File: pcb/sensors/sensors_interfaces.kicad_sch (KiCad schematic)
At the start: 26 parts, among them J3 CAN BUS, J4 DIMMER / GROVE, J5 XDB401 / GROVE, J6 DIGMESA / FLOW, J7 M5STACK VALVE SSR, J8 BOILER SSR / 5V OUT, Q2 AO3401A, Q3 2N7002, U4 TJA1051T/3, U5 TMP102AIDRLR

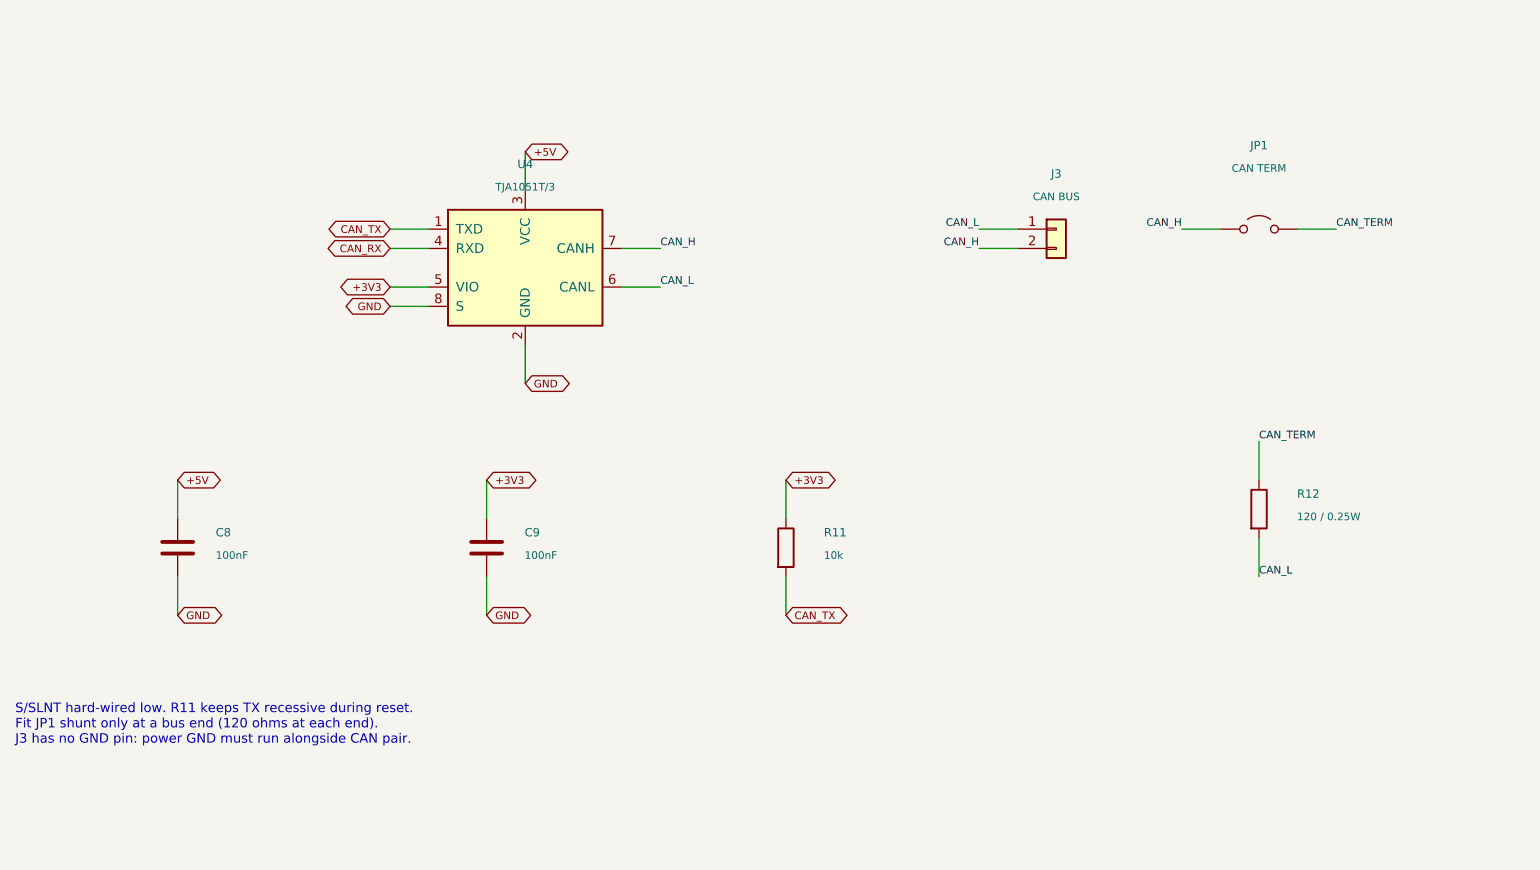
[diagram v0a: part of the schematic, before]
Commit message: Make sensors CAN termination permanent and consolidate PCB ignores
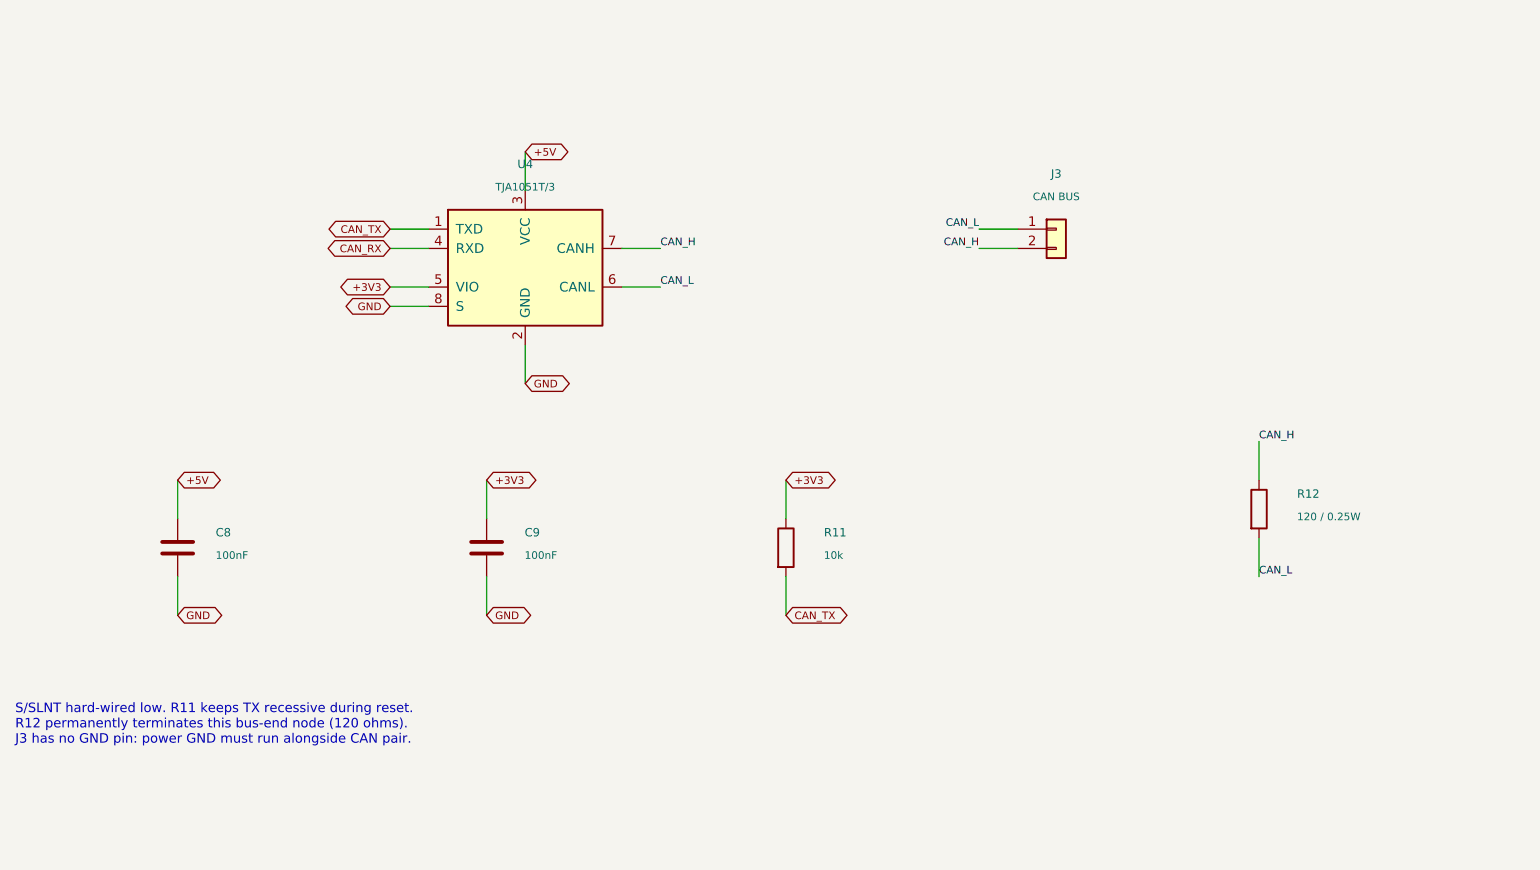
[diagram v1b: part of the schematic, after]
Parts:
- removed JP1: CAN TERM, Connector_PinHeader_2.54mm:PinHeader_1x02_P2.54mm_Vertical, symbol Jumper:Jumper_2_Open
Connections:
- net CAN_TERM is gone; now on net CAN_H: R12.1
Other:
- note added: "S/SLNT hard-wired low. R11 keeps TX recessive during reset. R12 permanently terminates this bus-end node (120 ohms). J3 has no GND pin: power GND must run alongside CAN pair."
- note removed: "S/SLNT hard-wired low. R11 keeps TX recessive during reset. Fit JP1 shunt only at a bus end (120 ohms at each end). J3 has no GND pin: power GND must run alongside CAN pair."
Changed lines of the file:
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@@
 (global_label "CAN_TX" (shape bidirectional) (at 119.38 100.33 0) (effects (font (size 1.0 1.0)) (justify left)) (property "Intersheetrefs" "${INTERSHEET_REFS}" (at 119.38 100.33 0) (hide yes) (effects (font (size 1.0 1.0)))))
 (symbol (lib_id "Device:R") (at 119.38 91.44 0) (unit 1) (exclude_from_sim no) (in_bom yes) (on_board yes) (dnp no) (property "Reference" "R11" (at 124.38 89.44 0) (effects (font (size 1.1 1.1)) (justify left))) (property "Value" "10k" (at 124.38 92.44 0) (effects (font (size 1.0 1.0)) (justify left))) (property "Footprint" "Resistor_SMD:R_0603_1608Metric" (at 119.38 91.44 0) (effects (font (size 1.0 1.0)) (justify left)) (hide yes)) (property "Datasheet" "" (at 119.38 91.44 0) (effects (font (size 1.0 1.0)) (justify left)) (hide yes)) (property "Description" "Resistor" (at 119.38 91.44 0) (effects (font (size 1.0 1.0)) (justify left)) (hide yes)) (property "MPN" "Generic 10k 1% 0603" (at 119.38 91.44 0) (effects (font (size 1.0 1.0)) (justify left)) (hide yes)) (pin "1") (pin "2") (instances (project "sensors" (path "/655ba0f3-0427-5cf4-88d9-0bb38b1023d4/75feafe7-4600-5614-9e51-33ca428cd046" (reference "R11") (unit 1)))))
-(wire (pts (xy 176.53 49.53) (xy 171.45 49.53)) (stroke (width 0) (type default)))
-(label "CAN_H" (at 171.45 49.53 0) (effects (font (size 1.0 1.0)) (justify right bottom)))
-(wire (pts (xy 186.69 49.53) (xy 191.77 49.53)) (stroke (width 0) (type default)))
-(label "CAN_TERM" (at 191.77 49.53 0) (effects (font (size 1.0 1.0)) (justify left bottom)))
-(symbol (lib_id "Jumper:Jumper_2_Open") (at 181.61 49.53 0) (unit 1) (exclude_from_sim no) (in_bom yes) (on_board yes) (dnp no) (property "Reference" "JP1" (at 181.61 38.53 0) (effects (font (size 1.1 1.1)))) (property "Value" "CAN TERM" (at 181.61 41.53 0) (effects (font (size 1.0 1.0)))) (property "Footprint" "Connector_PinHeader_2.54mm:PinHeader_1x02_P2.54mm_Vertical" (at 181.61 49.53 0) (effects (font (size 1.0 1.0))) (hide yes)) (property "Datasheet" "" (at 181.61 49.53 0) (effects (font (size 1.0 1.0))) (hide yes)) (property "Description" "Jumper, 2-pole, open" (at 181.61 49.53 0) (effects (font (size 1.0 1.0))) (hide yes)) (property "MPN" "2.54mm 2-pin header + removable shunt" (at 181.61 49.53 0) (effects (font (size 1.0 1.0))) (hide yes)) (pin "1") (pin "2") (instances (project "sensors" (path "/655ba0f3-0427-5cf4-88d9-0bb38b1023d4/75feafe7-4600-5614-9e51-33ca428cd046" (reference "JP1") (unit 1)))))
 (wire (pts (xy 181.61 82.55) (xy 181.61 77.47)) (stroke (width 0) (type default)))
-(label "CAN_TERM" (at 181.61 77.47 0) (effects (font (size 1.0 1.0)) (justify left bottom)))
+(label "CAN_H" (at 181.61 77.47 0) (effects (font (size 1.0 1.0)) (justify left bottom)))
 (wire (pts (xy 181.61 90.17) (xy 181.61 95.25)) (stroke (width 0) (type default)))
 (label "CAN_L" (at 181.61 95.25 0) (effects (font (size 1.0 1.0)) (justify left bottom)))
 (symbol (lib_id "Device:R") (at 181.61 86.36 0) (unit 1) (exclude_from_sim no) (in_bom yes) (on_board yes) (dnp no) (property "Reference" "R12" (at 186.61 84.36 0) (effects (font (size 1.1 1.1)) (justify left))) (property "Value" "120 / 0.25W" (at 186.61 87.36 0) (effects (font (size 1.0 1.0)) (justify left))) (property "Footprint" "Resistor_SMD:R_1206_3216Metric" (at 181.61 86.36 0) (effects (font (size 1.0 1.0)) (justify left)) (hide yes)) (property "Datasheet" "" (at 181.61 86.36 0) (effects (font (size 1.0 1.0)) (justify left)) (hide yes)) (property "Description" "Resistor" (at 181.61 86.36 0) (effects (font (size 1.0 1.0)) (justify left)) (hide yes)) (property "MPN" "Generic 120 / 0.25W 1% 1206" (at 181.61 86.36 0) (effects (font (size 1.0 1.0)) (justify left)) (hide yes)) (pin "1") (pin "2") (instances (project "sensors" (path "/655ba0f3-0427-5cf4-88d9-0bb38b1023d4/75feafe7-4600-5614-9e51-33ca428cd046" (reference "R12") (unit 1)))))
-(text "S/SLNT hard-wired low. R11 keeps TX recessive during reset.\nFit JP1 shunt only at a bus end (120 ohms at each end).\nJ3 has no GND pin: power GND must run alongside CAN pair." (at 18 112 0) (effects (font (size 1.25 1.25)) (justify left top)))
+(text "S/SLNT hard-wired low. R11 keeps TX recessive during reset.\nR12 permanently terminates this bus-end node (120 ohms).\nJ3 has no GND pin: power GND must run alongside CAN pair." (at 18 112 0) (effects (font (size 1.25 1.25)) (justify left top)))
 (text "5. SHARED I2C - 3.3V, Grove/HY2.0 cable order" (at 230 15 0) (effects (font (size 1.7 1.7)) (justify left top)))
 (wire (pts (xy 373.38 41.91) (xy 368.3 41.91)) (stroke (width 0) (type default)))

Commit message: manual PCB design
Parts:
- removed C11, C13: 100nF, Capacitor_SMD:C_0603_1608Metric, symbol Device:C
- removed J5: XDB401 / GROVE, Connector:NS-Tech_Grove_1x04_P2mm_Vertical, symbol Connector_Generic:Conn_01x04
- J4: value DIMMER / GROVE -> DIMMER I2C
- J6: value DIGMESA / FLOW -> FLOW HALL
- J7: value M5STACK VALVE SSR -> VALVE SSR
- J8: value BOILER SSR / 5V OUT -> BOILER SSR
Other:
- note added: "GPIO36, 3.3V signal / 5V VCC; default LOW."
- note added: "GPIO41 input; internal pull-up disabled. 1k x 10nF = 10us. Digmesa powered from 5V; signal pulled to 3.3V only. Pin order: GND brown / 5V green / SIGNAL yellow. RC discharge speed also depends on sensor/cable impedance."
- note added: "Grove opening up: left-to-right GND / 3V3 / SDA / SCL. Numbered pads: 1=SCL yellow, 2=SDA white, 3=3V3 red, 4=GND black. Addresses: dimmer 0x50 / XDB401 0x7F / TMP102 0x48. TMP102 ADD0 grounded; ALERT unused. Mount away from LDO heat. Pull-ups always fitted: 2.35k effective with XDB401 attached. 100kHz initial bus speed; remote modules provide local supply decoupling."
- note removed: "GPIO4 input; internal pull-up disabled. 1k x 10nF = 10us. Digmesa powered from 5V; signal pulled to 3.3V only. Pin order: GND brown / 5V green / SIGNAL yellow. RC discharge speed also depends on sensor/cable impedance."
- note removed: "GPIO9, 3.3V signal / 5V VCC; default LOW."
- note removed: "Grove opening up: left-to-right GND / 3V3 / SDA / SCL. Numbered pads: 1=SCL yellow, 2=SDA white, 3=3V3 red, 4=GND black. Addresses: dimmer 0x50 / XDB401 0x7F / TMP102 0x48. TMP102 ADD0 grounded; ALERT unused. Mount away from LDO heat. Pull-ups always fitted: 2.35k effective with XDB401 attached. 100kHz initial bus speed; C11 bypasses connector supply."

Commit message: Finalize sensors PCB and JLCPCB manufacturing exports
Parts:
- C10, C8, C9: LCSC (none) -> C14663; MPN Generic 100nF X7R >=10V -> CC0603KRX7R9BB104
- C12: LCSC (none) -> C57112; MPN Generic 10nF X7R >=10V -> 0603B103K500NT
- J3, J8: LCSC (none) -> C158012; MPN JST B2B-XH-A -> B2B-XH-A(LF)(SN)
- J4: footprint Connector:NS-Tech_Grove_1x04_P2mm_Vertical -> Sensors_Local:CONN-TH_HY-4A; LCSC (none) -> C722737; MPN NS-Tech Grove vertical HY2.0-4P -> HY-4A
- J6, J7: LCSC (none) -> C144394; MPN JST B3B-XH-A -> B3B-XH-A(LF)(SN)
- Q2: LCSC (none) -> C15127
- Q3: LCSC (none) -> C8545
- R11, R17, R21: LCSC (none) -> C25804; MPN Generic 10k 1% 0603 -> 0603WAF1002T5E
- R12: LCSC (none) -> C17909; MPN Generic 120 / 0.25W 1% 1206 -> 1206W4F1200T5E
- R13, R14: LCSC (none) -> C23162; MPN Generic 4.7k 1% 0603 -> 0603WAF4701T5E
- R15, R22: LCSC (none) -> C21190; MPN Generic 1k 1% 0603 -> 0603WAF1001T5E
- R19: LCSC (none) -> C25803; MPN Generic 100k 1% 0603 -> 0603WAF1003T5E
- U4: LCSC (none) -> C38695; MPN TJA1051T/3,118 -> TJA1051T/3/1J
- U5: LCSC (none) -> C99269
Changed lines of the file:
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@@
 			)
 		)
-		(property "MPN" "JST B3B-XH-A"
+		(property "MPN" "B3B-XH-A(LF)(SN)"
 			(at 378.46 185.42 0)
 			(hide yes)
@@
 			)
 		)
+		(property "LCSC" "C144394" (at 378.46 185.42 0) (hide yes) (effects (font (size 1 1))))
 	)
 	(symbol
@@
 			)
 		)
-		(property "MPN" "Generic 100k 1% 0603"
+		(property "MPN" "0603WAF1003T5E"
 			(at 25.4 250.19 0)
 			(hide yes)
@@
 			)
 		)
+		(property "LCSC" "C25803" (at 25.4 250.19 0) (hide yes) (effects (font (size 1 1))))
 	)
 	(symbol
@@
 			)
 		)
-		(property "MPN" "Generic 1k 1% 0603"
+		(property "MPN" "0603WAF1001T5E"
 			(at 255.27 267.97 0)
 			(hide yes)
@@
 			)
 		)
+		(property "LCSC" "C21190" (at 255.27 267.97 0) (hide yes) (effects (font (size 1 1))))
 	)
 	(symbol
@@
 			)
 		)
-		(property "MPN" "Generic 1k 1% 0603"
+		(property "MPN" "0603WAF1001T5E"
 			(at 110.49 173.99 0)
 			(hide yes)
@@
 			)
 		)
+		(property "LCSC" "C21190" (at 110.49 173.99 0) (hide yes) (effects (font (size 1 1))))
 	)
 	(symbol
@@
 			)
 		)
+		(property "LCSC" "C99269" (at 279.4 95.25 0) (hide yes) (effects (font (size 1 1))))
 	)
 	(symbol
@@
 			)
 		)
-		(property "MPN" "JST B3B-XH-A"
+		(property "MPN" "B3B-XH-A(LF)(SN)"
 			(at 48.26 176.53 0)
 			(hide yes)
@@
 			)
 		)
+		(property "LCSC" "C144394" (at 48.26 176.53 0) (hide yes) (effects (font (size 1 1))))
 	)
 	(symbol
@@
 			)
 		)
-		(property "MPN" "Generic 10k 1% 0603"
+		(property "MPN" "0603WAF1002T5E"
 			(at 119.38 91.44 0)
 			(hide yes)
@@
 			)
 		)
+		(property "LCSC" "C25804" (at 119.38 91.44 0) (hide yes) (effects (font (size 1 1))))
 	)
 	(symbol
@@
 			)
 		)
-		(property "Footprint" "Connector:NS-Tech_Grove_1x04_P2mm_Vertical"
+		(property "Footprint" "Sensors_Local:CONN-TH_HY-4A"
 			(at 378.46 44.45 0)
 			(hide yes)
@@
 			)
 		)
-		(property "MPN" "NS-Tech Grove vertical HY2.0-4P"
+		(property "MPN" "HY-4A"
 			(at 378.46 44.45 0)
 			(hide yes)
@@
 			)
 		)
+		(property "LCSC" "C722737" (at 378.46 44.45 0) (hide yes) (effects (font (size 1 1))))
 	)
 	(symbol
@@
 			)
 		)
-		(property "MPN" "Generic 10nF X7R >=10V"
+		(property "MPN" "0603B103K500NT"
 			(at 154.94 173.99 0)
 			(hide yes)
@@
 			)
 		)
+		(property "LCSC" "C57112" (at 154.94 173.99 0) (hide yes) (effects (font (size 1 1))))
 	)
 	(symbol
@@
 			)
 		)
-		(property "MPN" "Generic 4.7k 1% 0603"
+		(property "MPN" "0603WAF4701T5E"
 			(at 242.57 46.99 0)
 			(hide yes)
@@
 			)
 		)
+		(property "LCSC" "C23162" (at 242.57 46.99 0) (hide yes) (effects (font (size 1 1))))
 	)
 	(symbol
@@
 			)
 		)
-		(property "MPN" "JST B2B-XH-A"
+		(property "MPN" "B2B-XH-A(LF)(SN)"
 			(at 154.94 49.53 0)
 			(hide yes)
@@
 			)
 		)
+		(property "LCSC" "C158012" (at 154.94 49.53 0) (hide yes) (effects (font (size 1 1))))
 	)
 	(symbol
@@
 			)
 		)
-		(property "MPN" "Generic 100nF X7R >=10V"
+		(property "MPN" "CC0603KRX7R9BB104"
 			(at 39.37 91.44 0)
 			(hide yes)
@@
 			)
 		)
+		(property "LCSC" "C14663" (at 39.37 91.44 0) (hide yes) (effects (font (size 1 1))))
 	)
 	(symbol
@@
 			)
 		)
-		(property "MPN" "Generic 4.7k 1% 0603"
+		(property "MPN" "0603WAF4701T5E"
 			(at 283.21 46.99 0)
 			(hide yes)
@@
 			)
 		)
+		(property "LCSC" "C23162" (at 283.21 46.99 0) (hide yes) (effects (font (size 1 1))))
 	)
 	(symbol
@@
 			)
 		)
-		(property "MPN" "Generic 100nF X7R >=10V"
+		(property "MPN" "CC0603KRX7R9BB104"
 			(at 325.12 115.57 0)
 			(hide yes)
@@
 			)
 		)
+		(property "LCSC" "C14663" (at 325.12 115.57 0) (hide yes) (effects (font (size 1 1))))
 	)
 	(symbol
@@
 			)
 		)
+		(property "LCSC" "C15127" (at 224.79 245.11 0) (hide yes) (effects (font (size 1 1))))
 	)
 	(symbol
@@
 			)
 		)
-		(property "MPN" "Generic 100nF X7R >=10V"
+		(property "MPN" "CC0603KRX7R9BB104"
 			(at 80.01 91.44 0)
 			(hide yes)
@@
 			)
 		)
+		(property "LCSC" "C14663" (at 80.01 91.44 0) (hide yes) (effects (font (size 1 1))))
 	)
 	(symbol
@@
 			)
 		)
-		(property "MPN" "TJA1051T/3,118"
+		(property "MPN" "TJA1051T/3/1J"
 			(at 85.09 54.61 0)
 			(hide yes)
@@
 			)
 		)
+		(property "LCSC" "C38695" (at 85.09 54.61 0) (hide yes) (effects (font (size 1 1))))
 	)
 	(symbol
@@
 			)
 		)
-		(property "MPN" "Generic 10k 1% 0603"
+		(property "MPN" "0603WAF1002T5E"
 			(at 322.58 190.5 0)
 			(hide yes)
@@
 			)
 		)
+		(property "LCSC" "C25804" (at 322.58 190.5 0) (hide yes) (effects (font (size 1 1))))
 	)
 	(symbol
@@
 			)
 		)
+		(property "LCSC" "C8545" (at 69.85 250.19 0) (hide yes) (effects (font (size 1 1))))
 	)
 	(symbol
@@
 			)
 		)
-		(property "MPN" "JST B2B-XH-A"
+		(property "MPN" "B2B-XH-A(LF)(SN)"
 			(at 288.29 242.57 0)
 			(hide yes)
@@
 			)
 		)
+		(property "LCSC" "C158012" (at 288.29 242.57 0) (hide yes) (effects (font (size 1 1))))
 	)
 	(symbol
@@
 			)
 		)
-		(property "MPN" "Generic 120 / 0.25W 1% 1206"
+		(property "MPN" "1206W4F1200T5E"
 			(at 181.61 86.36 0)
 			(hide yes)
@@
 			)
 		)
+		(property "LCSC" "C17909" (at 181.61 86.36 0) (hide yes) (effects (font (size 1 1))))
 	)
 	(symbol
@@
 			)
 		)
-		(property "MPN" "Generic 10k 1% 0603"
+		(property "MPN" "0603WAF1002T5E"
 			(at 175.26 267.97 0)
 			(hide yes)
@@
 			)
 		)
+		(property "LCSC" "C25804" (at 175.26 267.97 0) (hide yes) (effects (font (size 1 1))))
 	)
 	(sheet_instances

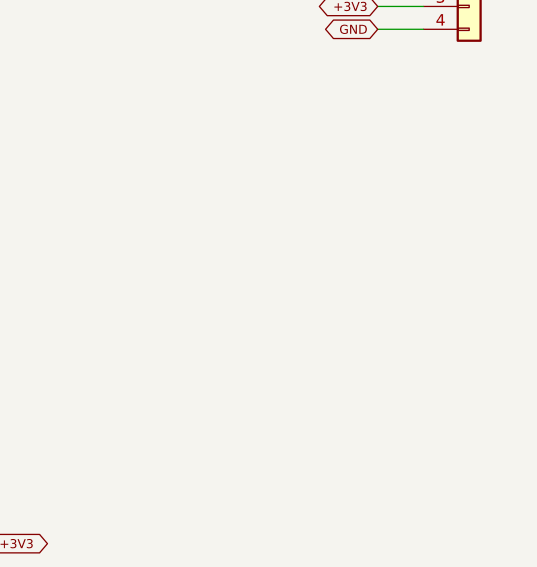
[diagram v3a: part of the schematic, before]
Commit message: Add Grove I2C passthrough board and update sensors manufacturing
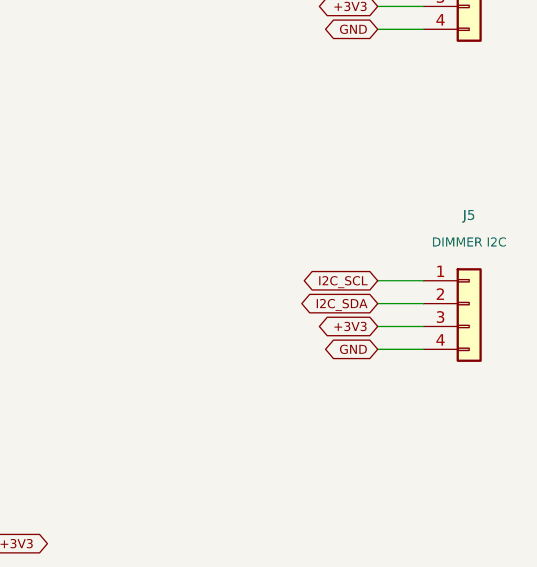
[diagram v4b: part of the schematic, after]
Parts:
- added J5: DIMMER I2C, Sensors_Local:CONN-TH_HY-4A, symbol Connector_Generic:Conn_01x04
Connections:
- net +3V3: now also J5.3 (Pin_3)
- net GND: now also J5.4 (Pin_4)
- net I2C_SCL: now also J5.1 (Pin_1)
- net I2C_SDA: now also J5.2 (Pin_2)
